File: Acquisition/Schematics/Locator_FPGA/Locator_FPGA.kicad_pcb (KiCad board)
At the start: 4 copper layers, 72.9 x 42.2 mm, 138 parts, among them J1 Conn_02x07_Odd_Even, J2 USB_A, J3 Conn_02x12_Odd_Even, J4 2004850720, J5 Conn_02x03_Odd_Even, J6 OUTPUT Barrel, J7 Conn_01x02, J8 2004850720, Q1 IRLML9301, SW1 SW_DIP_x08, U1 XC6SLX9-TQG144, U2 M25PX32-VMW, U4 USB3300-EZK, U6 STM32F407VETx, U7 AMS1117, U8 AMS1117, U9 M95256-WMN6P, X1 XO91, Y1 Crystal, Y2 Crystal_GND24

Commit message: Schematics - FPGA board seems done
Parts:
- removed D7: LED, LED_SMD:LED_0805_2012Metric
- added R33: 30, Resistor_SMD:R_0603_1608Metric, F.Cu at (49.5, 35.8)
- added RN1: R_Pack04, Resistor_SMD:R_Array_Concave_4x0402, F.Cu at (49.6, 39.1)
- added RN2: R_Pack04, Resistor_SMD:R_Array_Concave_4x0402, B.Cu at (65.3, 33.7)
- added RN3: R_Pack04, Resistor_SMD:R_Array_Concave_4x0402, B.Cu at (69.0, 39.5)
- added U3: M95256-WMN6P, Package_SO:SOIC-8_3.9x4.9mm_P1.27mm, F.Cu at (43.8, 37.5)
- J6: footprint Connector_BarrelJack:BarrelJack_Horizontal -> Connector_PinHeader_2.54mm:PinHeader_1x02_P2.54mm_Vertical; moved to F.Cu
- R24: value 0 -> 30; moved to F.Cu
- R25: value 0 -> 30
- R29: value 200R -> 30
- moved R29 35.0 mm to (64.9, 31.5), turned to 180 degrees
- moved R24 13.2 mm to (49.5, 37.2), turned to 180 degrees
- moved R25 9.91 mm to (64.9, 30.0), turned to 0 degrees
- moved D8 6.94 mm to (48.1, 44.6), turned to -90 degrees
- moved J6 6.63 mm to (45.6, 48.0)
- moved R5 4.23 mm to (61.3, 29.1)
- moved C19 3.60 mm to (39.8, 43.3), turned to 90 degrees
- moved R18 1.65 mm to (42.7, 41.0)
- moved C20 1.61 mm to (42.7, 42.5)
- moved C7 1.15 mm to (32.9, 47.4)
- moved J3 0.93 mm to (53.8, 17.5)
- moved C5 0.23 mm to (29.3, 47.1)
- moved C29 0.07 mm to (63.6, 25.3)
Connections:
- net /ADC_PAR_D1 renamed /FSMC_DA2
- net /ADC_PAR_D2 renamed /FSMC_DA3
- net /MicArray/MISO1 renamed /MicArray/CamVSYNC
- net /MicArray/MISO10 renamed /MicArray/CamPCLK
- net /MicArray/MISO11 renamed /MicArray/CamD4
- net /MicArray/MISO12 renamed /MicArray/CamD0
- net /MicArray/MISO13 renamed /MicArray/CamD1
- net /MicArray/MISO2 renamed /MicArray/CamD6
- net /MicArray/MISO3 renamed /MicArray/CamMCLK
- net /MicArray/MISO4 renamed /MicArray/CamHSYNC
- net /MicArray/MISO5 renamed /MicArray/CamD2
- net /MicArray/MISO6 renamed /MicArray/CamD3
- net /MicArray/MISO7 renamed /MicArray/CamSDA
- net /MicArray/MISO8 renamed /MicArray/CamD7
- net /MicArray/MOSI renamed /MicArray/CamSCK
- D1 pad 2: /MicArray/DONE -> /DONE
- J3 pad 13: /MicArray/MISO9 -> /MicArray/CamD5
- J3 pad 3: /MicArray/SCLK -> /MicArray/CamPWDN
- J3 pad 4: /MicArray/CONVST -> /MicArray/CamRST
- J4 pad 17: /MicArray/FFC2_21 -> /MicArray/ADC_SDI
- J4 pad 18: /MicArray/FFC2_22 -> /MicArray/ADC_SCK
- J4 pad 19: /MicArray/FFC2_23 -> /MicArray/ADC_MCLK
- J8 pad 2: /MicArray/FFC3_06 -> /MicArray/ADC_MCLK
- J8 pad 3: /MicArray/FFC3_07 -> /MicArray/ADC_SCK
- J8 pad 4: /MicArray/FFC3_08 -> /MicArray/ADC_SDI
- R24 pad 1: /MicArray/CONVST -> /MicArray/EEPROM2_nH
- R24 pad 2: /MicArray/FFC2_22 -> Net-(U3-~{HOLD})
- R25 pad 1: /MicArray/SCLK -> /MicArray/EEPROM_nH
- R25 pad 2: /MicArray/FFC2_23 -> Net-(U9-D)
- R29 pad 1: +3.3V -> Net-(U9-C)
- R29 pad 2: Net-(D7-A) -> /MicArray/EEPROM_C
- R8 pad 2: /MicArray/DONE -> /DONE
- U1 pad 104: /MicArray/CONVST -> /MicArray/CamRST
- U1 pad 105: /MicArray/SCLK -> /MicArray/CamPWDN
- U1 pad 111: /ADC_PAR_D3 -> /FSMC_NL
- U1 pad 115: /ADC_PAR_D4 -> /MicArray/SW5
- U1 pad 116: /ADC_PAR_D5 -> /MicArray/SW4
- U1 pad 117: /ADC_PAR_D6 -> /STATUS
- U1 pad 118: /ADC_PAR_D7 -> unconnected-(U1A-IO_L63N_SCP6_0-Pad118)
- U1 pad 119: /ADC_PAR_D8 -> /MicArray/FFC2_19
- U1 pad 120: /MicArray/FFC2_19 -> /MicArray/FFC2_20
- U1 pad 121: /ADC_DIN -> /FSMC_NWAIT
- U1 pad 123: /ADC_CLK -> /FSMC_NWE
- U1 pad 124: /ADC_BSY -> /FSMC_DA1
- U1 pad 126: /MicArray/FFC2_20 -> /FSMC_DA0
- U1 pad 127: /MicArray/FFC2_21 -> /FSMC_NE1
- U1 pad 131: /FPGA_additional_1 -> /MicArray/EEPROM2_nS
- U1 pad 132: /FPGA_additional_2 -> /MicArray/EEPROM2_nH
- U1 pad 133: /ADC_PAR_D16 -> /MicArray/EEPROM2_Q
- U1 pad 134: /ADC_PAR_D15 -> /MicArray/EEPROM2_C
- U1 pad 137: /ADC_PAR_D14 -> /MicArray/EEPROM2_D
- U1 pad 138: /ADC_PAR_D13 -> /MicArray/EEPROM2_nW
- U1 pad 139: /ADC_PAR_D12 -> /FSMC_DA7
- U1 pad 140: /ADC_PAR_D11 -> /FSMC_DA6
- U1 pad 141: /ADC_PAR_D10 -> /FSMC_DA5
- U1 pad 142: /ADC_PAR_D9 -> /FSMC_DA4
- U1 pad 48: /MicArray/FFC3_06 -> Net-(RN3-R4.1)
- U1 pad 50: /MicArray/FFC3_07 -> Net-(RN3-R3.1)
- U1 pad 51: /MicArray/FFC3_08 -> Net-(RN3-R1.1)
- U1 pad 71: /MicArray/DONE -> /DONE
- U1 pad 93: /MicArray/SW4 -> /MicArray/CamD5
- U1 pad 94: /MicArray/SW5 -> /FSMC_NOE
- U1 pad 95: /MicArray/MISO9 -> /FSMC_CLK
- U6 pad 32: /ADC_DIN -> /MOSI_1
- U6 pad 38: Earth -> /FSMC_DA4
- U6 pad 39: Earth -> /FSMC_DA5
- U6 pad 40: Earth -> /FSMC_DA6
- U6 pad 41: Earth -> /FSMC_DA7
- U6 pad 61: /ADC_PAR_D15 -> /FSMC_DA0
- U6 pad 62: /ADC_PAR_D16 -> /FSMC_DA1
- U6 pad 63: /FPGA_additional_2 -> unconnected-(U6-PC6-Pad63)
- U6 pad 64: /FPGA_additional_1 -> unconnected-(U6-PC7-Pad64)
- U6 pad 65: /ADC_BSY -> unconnected-(U6-PC8-Pad65)
- U6 pad 67: /ADC_CLK -> unconnected-(U6-PA8-Pad67)
- U6 pad 68: /ADC_CS2 -> /DONE
- U6 pad 69: unconnected-(U6-PA10-Pad69) -> /STATUS
- U6 pad 83: /ADC_PAR_D3 -> unconnected-(U6-PD2-Pad83)
- U6 pad 84: /ADC_PAR_D4 -> /FSMC_CLK
- U6 pad 85: /ADC_PAR_D5 -> /FSMC_NOE
- U6 pad 86: /ADC_PAR_D6 -> /FSMC_NWE
- U6 pad 87: /ADC_PAR_D7 -> /FSMC_NWAIT
- U6 pad 88: /ADC_PAR_D8 -> /FSMC_NE1
- U6 pad 93: /LED6 -> /FSMC_NL
- U9 pad 1: /MicArray/EEPROM_nS -> Net-(RN2-R2.1)
- U9 pad 2: /MicArray/EEPROM_Q -> Net-(RN2-R3.1)
- U9 pad 3: /MicArray/EEPROM_nW -> Net-(RN2-R4.1)
- U9 pad 5: /MicArray/EEPROM_D -> Net-(U9-D)
- U9 pad 6: /MicArray/EEPROM_C -> Net-(U9-C)
- U9 pad 7: /MicArray/EEPROM_nH -> Net-(RN2-R1.1)
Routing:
- net /MicArray/ADC_MCLK: track 0.00 -> 70.1 mm, vias 0 -> 4
- net /MicArray/ADC_SCK: track 0.00 -> 61.7 mm, vias 0 -> 4
- net /MicArray/ADC_SDI: track 0.00 -> 60.2 mm, vias 0 -> 4
- net /DONE: track 0.00 -> 55.5 mm, vias 0 -> 2
- net /ADC_DIN: track 51.5 -> 0.00 mm, vias 2 -> 0
- net /MicArray/FFC2_22: track 42.0 -> 0.00 mm, vias 1 -> 0
- net /MicArray/FFC2_23: track 40.9 -> 0.00 mm, vias 1 -> 0
- net /FSMC_CLK: track 0.00 -> 36.1 mm, vias 0 -> 2
- net /FSMC_NOE: track 0.00 -> 36.0 mm, vias 0 -> 2
- net /MicArray/FFC2_21: track 35.0 -> 0.00 mm, vias 2 -> 0
- net /MicArray/FFC3_08: track 32.5 -> 0.00 mm, vias 2 -> 0
- net /FSMC_NL: track 0.00 -> 30.9 mm
- net /MicArray/FFC3_07: track 29.5 -> 0.00 mm, vias 2 -> 0
- net /ADC_BSY: track 29.3 -> 0.00 mm
- net /ADC_PAR_D8: track 27.7 -> 0.00 mm, vias 2 -> 0
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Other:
- board text added: "BIG BOI"
- board text added: "LIL BOI"

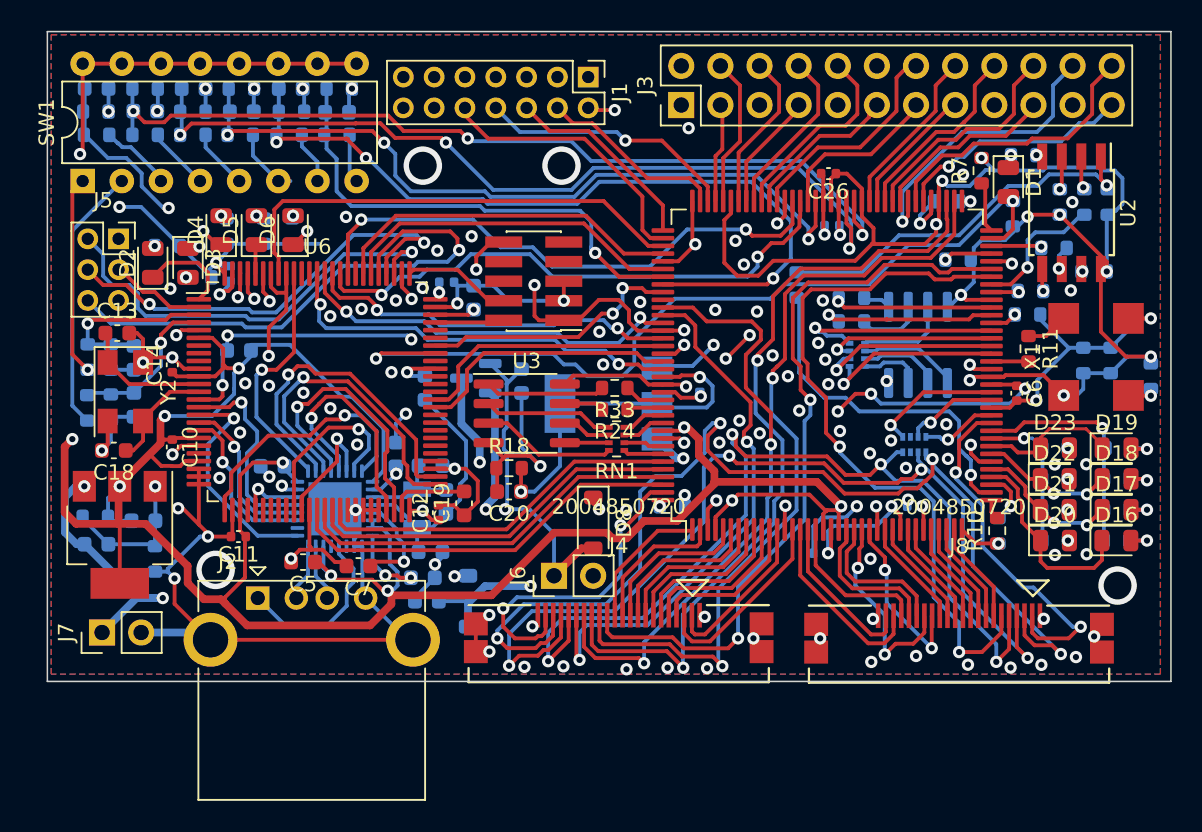
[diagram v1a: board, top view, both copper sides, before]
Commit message: Acquisition schematics should be working.
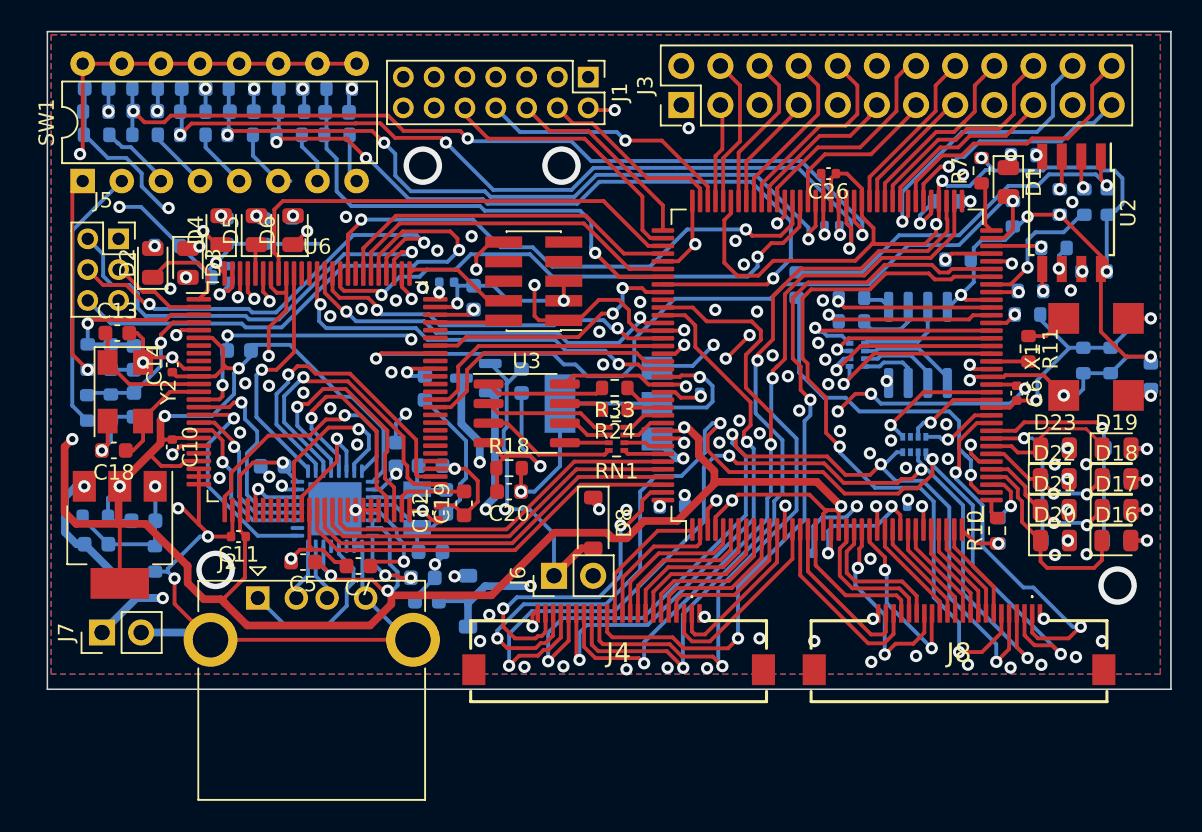
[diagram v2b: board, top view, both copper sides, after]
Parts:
- J4, J8: footprint footprints:CON_2004850720 -> CustomLibrary:Molex FFC 20pin sideways
- moved J4 0.90 mm to (49.8, 53.3)
- moved J8 0.87 mm to (71.9, 53.3)
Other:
- board size 72.9 x 42.2 mm -> 72.9 x 42.7 mm

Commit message: PCBs production ready
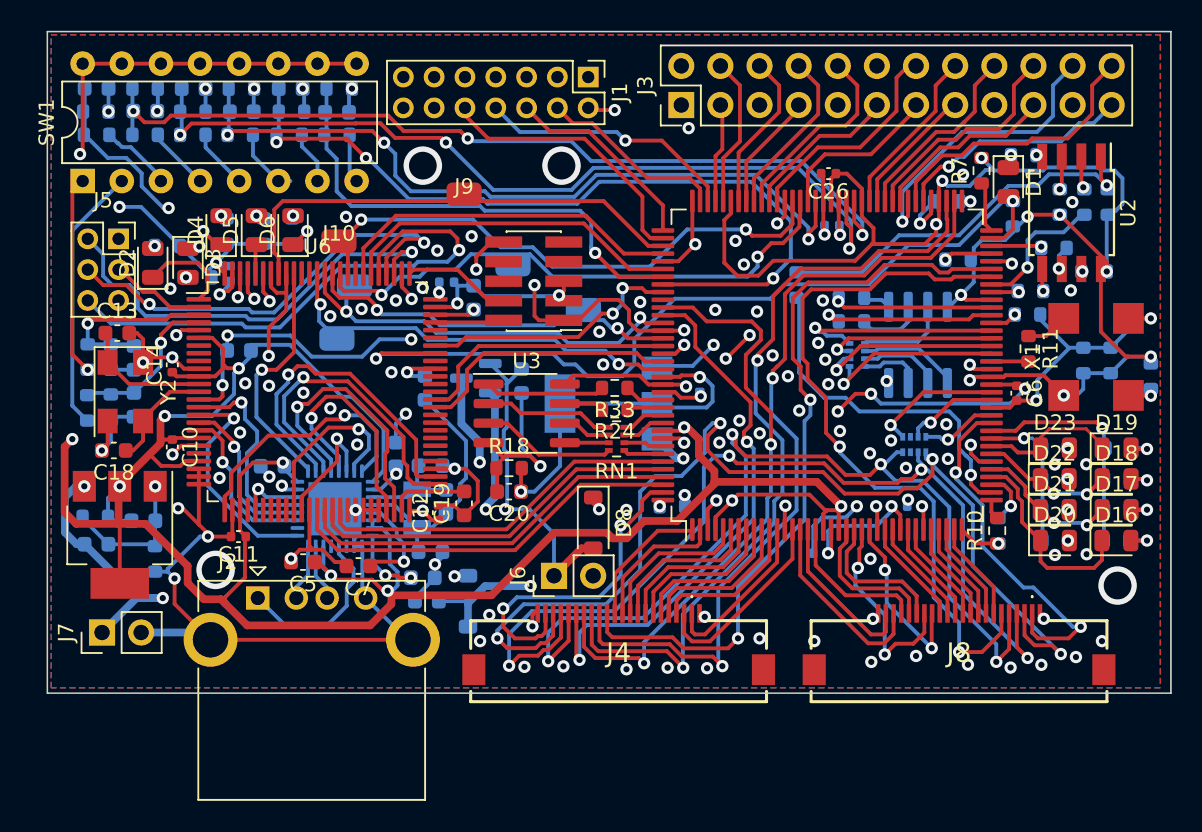
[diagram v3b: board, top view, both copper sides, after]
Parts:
- added J10: Pad, CustomLibrary:Pad, F.Cu at (31.6, 26.3)
- added J11: Pad, CustomLibrary:Pad, B.Cu at (32.6, 29.2)
- added J12: Pad, CustomLibrary:Pad, B.Cu at (42.9, 27.8)
- added J13: Pad, CustomLibrary:Pad, B.Cu at (47.5, 30.7)
- added J14: Pad, CustomLibrary:Pad, B.Cu at (31.5, 32.6)
- added J9: Pad, CustomLibrary:Pad, F.Cu at (39.8, 23.2)
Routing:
- net /FSMC_NWAIT: track 25.5 -> 27.4 mm
- net +3.3V: track 394.3 -> 392.5 mm
- net /NRST: track 28.4 -> 29.3 mm
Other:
- board size 72.9 x 42.7 mm -> 72.9 x 42.9 mm
- board text added: "CLK"
- board text added: "NE"
- board text added: "NL"
- board text added: "NOE"
- board text added: "NWAIT"
- board text added: "NWE"
- board text added: "SPEEDY BOI"
